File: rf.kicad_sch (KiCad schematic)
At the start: 13 parts, among them IC6 SI4468-A2A-IMR, Y1 TG2520SMN_30.000M-MCGNNM0

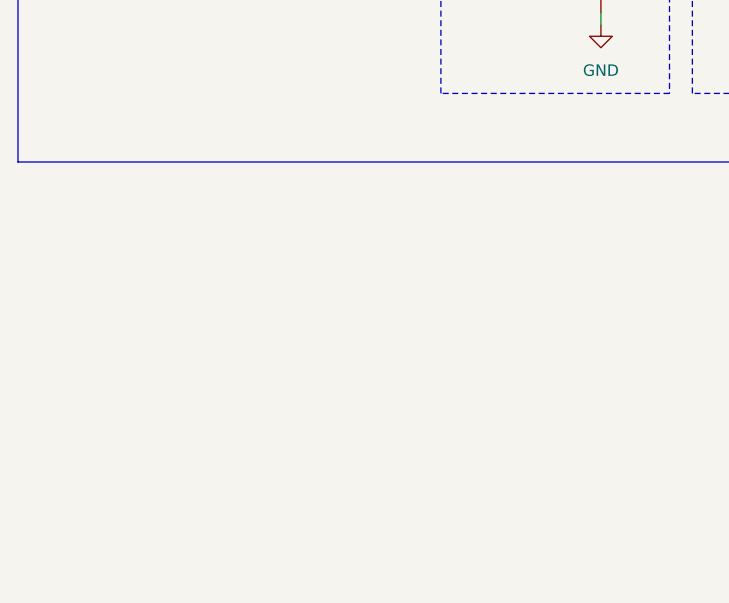
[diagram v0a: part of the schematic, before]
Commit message: RF switch design begun
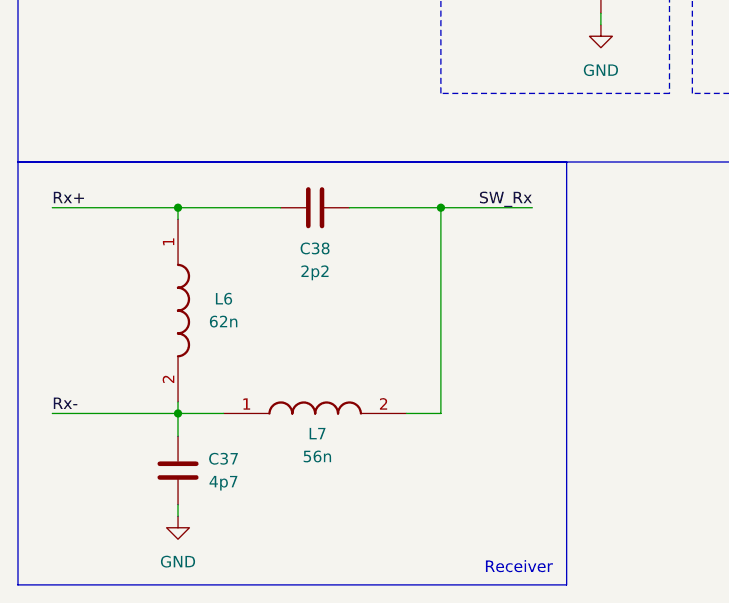
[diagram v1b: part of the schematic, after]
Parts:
- added C37: 4p7, Capacitor_SMD:C_0402_1005Metric, symbol Device:C
- added C38: 2p2, Capacitor_SMD:C_0402_1005Metric, symbol Device:C
- added L6: 62n, LQW15CNR20J00B, symbol SamacSys_Parts:LQW15AN20NG00D
- added L7: 56n, LQW15CNR20J00B, symbol SamacSys_Parts:LQW15AN20NG00D
- C34, C35: footprint (none) -> Capacitor_SMD:C_0402_1005Metric
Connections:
- net GND: now also C37.1
- net Rx+: now also C38.1, L6.1
- net Rx-: now also C37.2, L6.2, L7.1
- new net SW_Rx: C38.2, L7.2
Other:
- note added: "Receiver"
